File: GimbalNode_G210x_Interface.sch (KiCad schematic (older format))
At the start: 6 parts, among them P1 CONN_01X08_2MNT, P2 CONN_01X08_2MNT, U1 SN74HCT157D, U2 SN74HCT157D

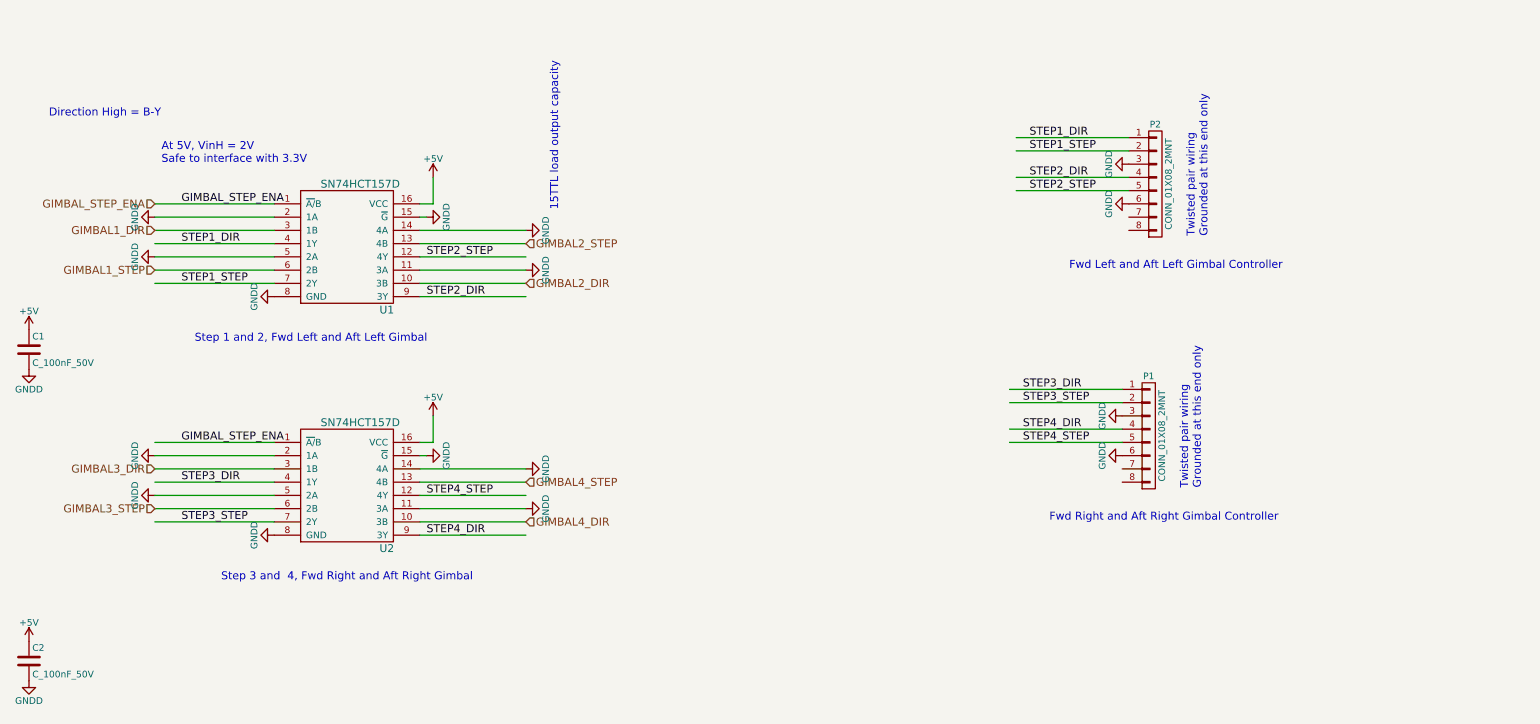
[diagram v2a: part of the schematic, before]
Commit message: Update connectors, diodes, add zener's and anotate.
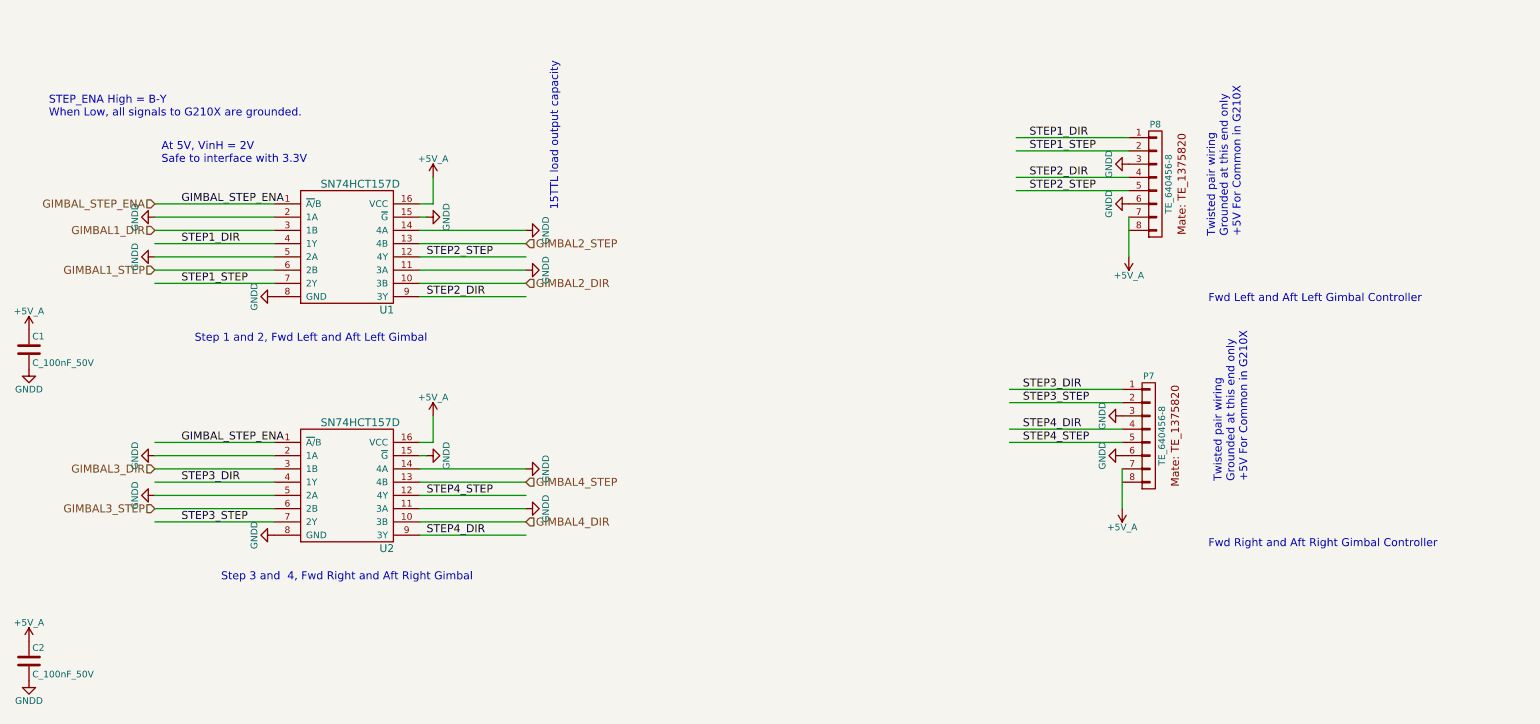
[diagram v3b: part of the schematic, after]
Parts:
- removed P1, P2: CONN_01X08_2MNT, symbol CONN_01X08_2MNT
- added P7, P8: TE_640456-8, RLOOP_FOOTPRINTS:rLoop_TE640456-8, symbol TE_640456-8
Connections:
- net labels added: +5V_A
- net labels removed: +5V
- wire segments 40 -> 42
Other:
- note added: "STEP_ENA High = B-Y\nWhen Low, all signals to G210X are grounded."
- note added: "Twisted pair wiring\nGrounded at this end only\n+5V For Common in G210X"
- note removed: "Direction High = B-Y"
- note removed: "Twisted pair wiring\nGrounded at this end only"
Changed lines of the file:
@@
 $Descr A3 16535 11693
 encoding utf-8
-Sheet 3 6
+Sheet 6 6
 Title "G210 Multiplexers"
 Date ""
@@
 Text Notes 11950 10350 0    118  ~ 0
 rLoop - Gimbal Node\nG210x Multiplexer Interface
-$Comp
-L CONN_01X08_2MNT P2
-U 1 1 5757EB8A
-P 12700 3150
-F 0 "P2" H 12700 3600 50  0000 C CNN
-F 1 "CONN_01X08_2MNT" V 12800 3150 50  0000 C CNN
-F 2 "" H 12700 3150 50  0000 C CNN
-F 3 "" H 12700 3150 50  0000 C CNN
-	1    12700 3150
-	1    0    0    -1
-$EndComp
 Text Notes 5450 4350 0    60   ~ 0
 Step 1 and 2, Fwd Left and Aft Left Gimbal
@@
 	12500 3200 11650 3200
 $Comp
-L GNDD #PWR25
+L GNDD #PWR0102
 U 1 1 5757EB8B
 P 12500 3000
-F 0 "#PWR25" H 12500 2750 50  0001 C CNN
+F 0 "#PWR0102" H 12500 2750 50  0001 C CNN
 F 1 "GNDD" H 12500 2850 50  0000 C CNN
 F 2 "" H 12500 3000 50  0000 C CNN
@@
 $EndComp
 $Comp
-L GNDD #PWR26
+L GNDD #PWR0103
 U 1 1 5757EB8C
 P 12500 3300
-F 0 "#PWR26" H 12500 3050 50  0001 C CNN
+F 0 "#PWR0103" H 12500 3050 50  0001 C CNN
 F 1 "GNDD" H 12500 3150 50  0000 C CNN
 F 2 "" H 12500 3300 50  0000 C CNN
@@
 Text Label 11750 3200 0    60   ~ 0
 STEP2_STEP
-Text Notes 13100 3550 1    60   ~ 0
-Twisted pair wiring\nGrounded at this end only
-$Comp
-L CONN_01X08_2MNT P1
-U 1 1 5757EB8D
-P 12650 5050
-F 0 "P1" H 12650 5500 50  0000 C CNN
-F 1 "CONN_01X08_2MNT" V 12750 5050 50  0000 C CNN
-F 2 "" H 12650 5050 50  0000 C CNN
-F 3 "" H 12650 5050 50  0000 C CNN
-	1    12650 5050
-	1    0    0    -1
-$EndComp
-Text Notes 12050 3800 0    60   ~ 0
+Text Notes 13350 3550 1    60   ~ 0
+Twisted pair wiring\nGrounded at this end only\n+5V For Common in G210X
+Text Notes 13100 4050 0    60   ~ 0
 Fwd Left and Aft Left Gimbal Controller
 Wire Wire Line
@@
 	12450 5100 11600 5100
 $Comp
-L GNDD #PWR23
+L GNDD #PWR0104
 U 1 1 5757EB8E
 P 12450 4900
-F 0 "#PWR23" H 12450 4650 50  0001 C CNN
+F 0 "#PWR0104" H 12450 4650 50  0001 C CNN
 F 1 "GNDD" H 12450 4750 50  0000 C CNN
 F 2 "" H 12450 4900 50  0000 C CNN
@@
 $EndComp
 $Comp
-L GNDD #PWR24
+L GNDD #PWR0105
 U 1 1 5757EB8F
 P 12450 5200
-F 0 "#PWR24" H 12450 4950 50  0001 C CNN
+F 0 "#PWR0105" H 12450 4950 50  0001 C CNN
 F 1 "GNDD" H 12450 5050 50  0000 C CNN
 F 2 "" H 12450 5200 50  0000 C CNN
@@
 Text Label 11700 5100 0    60   ~ 0
 STEP4_STEP
-Text Notes 13050 5450 1    60   ~ 0
-Twisted pair wiring\nGrounded at this end only
-Text Notes 11900 5700 0    60   ~ 0
+Text Notes 13400 5400 1    60   ~ 0
+Twisted pair wiring\nGrounded at this end only\n+5V For Common in G210X
+Text Notes 13100 5900 0    60   ~ 0
 Fwd Right and Aft Right Gimbal Controller
 Text Notes 12000 10500 0    60   ~ 0
@@
 	6050 3900 5150 3900
 $Comp
-L GNDD #PWR15
+L GNDD #PWR0106
 U 1 1 5757EB94
 P 7200 3400
-F 0 "#PWR15" H 7200 3150 50  0001 C CNN
+F 0 "#PWR0106" H 7200 3150 50  0001 C CNN
 F 1 "GNDD" H 7200 3250 50  0000 C CNN
 F 2 "" H 7200 3400 50  0000 C CNN
@@
 	7150 3400 7200 3400
 $Comp
-L GNDD #PWR13
+L GNDD #PWR0107
 U 1 1 5757EB95
 P 6050 4000
-F 0 "#PWR13" H 6050 3750 50  0001 C CNN
+F 0 "#PWR0107" H 6050 3750 50  0001 C CNN
 F 1 "GNDD" H 6050 3850 50  0000 C CNN
 F 2 "" H 6050 4000 50  0000 C CNN
@@
 Text Label 5350 3300 0    60   ~ 0
 GIMBAL_STEP_ENA
-$Comp
-L +5V #PWR17
-U 1 1 5757EB96
-P 7250 3100
-F 0 "#PWR17" H 7250 2950 50  0001 C CNN
-F 1 "+5V" H 7250 3240 50  0000 C CNN
-F 2 "" H 7250 3100 50  0000 C CNN
-F 3 "" H 7250 3100 50  0000 C CNN
-	1    7250 3100
-	1    0    0    -1
-$EndComp
 Wire Wire Line
 	7150 5100 7250 5100
@@
 	6050 5700 5150 5700
 $Comp
-L GNDD #PWR16
+L GNDD #PWR0108
 U 1 1 5757EB98
 P 7200 5200
-F 0 "#PWR16" H 7200 4950 50  0001 C CNN
+F 0 "#PWR0108" H 7200 4950 50  0001 C CNN
 F 1 "GNDD" H 7200 5050 50  0000 C CNN
 F 2 "" H 7200 5200 50  0000 C CNN
@@
 Text Label 5350 5100 0    60   ~ 0
 GIMBAL_STEP_ENA
-$Comp
-L +5V #PWR18
-U 1 1 5757EB9A
-P 7250 4900
-F 0 "#PWR18" H 7250 4750 50  0001 C CNN
-F 1 "+5V" H 7250 5040 50  0000 C CNN
-F 2 "" H 7250 4900 50  0000 C CNN
-F 3 "" H 7250 4900 50  0000 C CNN
-	1    7250 4900
-	1    0    0    -1
-$EndComp
 Text HLabel 5150 3300 0    60   Input ~ 0
 GIMBAL_STEP_ENA
@@
 GIMBAL4_DIR
 Text Notes 4350 2650 0    60   ~ 0
-Direction High = B-Y
+STEP_ENA High = B-Y\nWhen Low, all signals to G210X are grounded.
 Wire Wire Line
 	7150 3800 7950 3800
@@
 STEP4_STEP
 $Comp
-L GNDD #PWR9
+L GNDD #PWR0109
 U 1 1 5757F02C
 P 5150 3400
-F 0 "#PWR9" H 5150 3150 50  0001 C CNN
+F 0 "#PWR0109" H 5150 3150 50  0001 C CNN
 F 1 "GNDD" H 5150 3250 50  0000 C CNN
 F 2 "" H 5150 3400 50  0000 C CNN
@@
 $EndComp
 $Comp
-L GNDD #PWR10
+L GNDD #PWR0110
 U 1 1 5757F037
 P 5150 3700
-F 0 "#PWR10" H 5150 3450 50  0001 C CNN
+F 0 "#PWR0110" H 5150 3450 50  0001 C CNN
 F 1 "GNDD" H 5150 3550 50  0000 C CNN
 F 2 "" H 5150 3700 50  0000 C CNN
@@
 $EndComp
 $Comp
-L GNDD #PWR11
+L GNDD #PWR0111
 U 1 1 5757F042
 P 5150 5200
-F 0 "#PWR11" H 5150 4950 50  0001 C CNN
+F 0 "#PWR0111" H 5150 4950 50  0001 C CNN
 F 1 "GNDD" H 5150 5050 50  0000 C CNN
 F 2 "" H 5150 5200 50  0000 C CNN
@@
 $EndComp
 $Comp
-L GNDD #PWR12
+L GNDD #PWR0112
 U 1 1 5757F04D
 P 5150 5500
-F 0 "#PWR12" H 5150 5250 50  0001 C CNN
+F 0 "#PWR0112" H 5150 5250 50  0001 C CNN
 F 1 "GNDD" H 5150 5350 50  0000 C CNN
 F 2 "" H 5150 5500 50  0000 C CNN
@@
 $EndComp
 $Comp
-L GNDD #PWR19
+L GNDD #PWR0113
 U 1 1 5757F058
 P 7950 3500
-F 0 "#PWR19" H 7950 3250 50  0001 C CNN
+F 0 "#PWR0113" H 7950 3250 50  0001 C CNN
 F 1 "GNDD" H 7950 3350 50  0000 C CNN
 F 2 "" H 7950 3500 50  0000 C CNN
@@
 $EndComp
 $Comp
-L GNDD #PWR20
+L GNDD #PWR0114
 U 1 1 5757F063
 P 7950 3800
-F 0 "#PWR20" H 7950 3550 50  0001 C CNN
+F 0 "#PWR0114" H 7950 3550 50  0001 C CNN
 F 1 "GNDD" H 7950 3650 50  0000 C CNN
 F 2 "" H 7950 3800 50  0000 C CNN
@@
 $EndComp
 $Comp
-L GNDD #PWR21
+L GNDD #PWR0115
 U 1 1 5757F078
 P 7950 5300
-F 0 "#PWR21" H 7950 5050 50  0001 C CNN
+F 0 "#PWR0115" H 7950 5050 50  0001 C CNN
 F 1 "GNDD" H 7950 5150 50  0000 C CNN
 F 2 "" H 7950 5300 50  0000 C CNN
@@
 $EndComp
 $Comp
-L GNDD #PWR22
+L GNDD #PWR0116
 U 1 1 5757F083
 P 7950 5600
-F 0 "#PWR22" H 7950 5350 50  0001 C CNN
+F 0 "#PWR0116" H 7950 5350 50  0001 C CNN
 F 1 "GNDD" H 7950 5450 50  0000 C CNN
 F 2 "" H 7950 5600 50  0000 C CNN
@@
 $EndComp
 $Comp
-L GNDD #PWR14
+L GNDD #PWR0117
 U 1 1 5758A913
 P 6050 5800
-F 0 "#PWR14" H 6050 5550 50  0001 C CNN
+F 0 "#PWR0117" H 6050 5550 50  0001 C CNN
 F 1 "GNDD" H 6050 5650 50  0000 C CNN
 F 2 "" H 6050 5800 50  0000 C CNN
@@
 $EndComp
 $Comp
-L GNDD #PWR6
+L GNDD #PWR0118
 U 1 1 5758AA2C
 P 4200 4550
-F 0 "#PWR6" H 4200 4300 50  0001 C CNN
+F 0 "#PWR0118" H 4200 4300 50  0001 C CNN
 F 1 "GNDD" H 4200 4400 50  0000 C CNN
 F 2 "" H 4200 4550 50  0000 C CNN
@@
 $EndComp
 $Comp
-L +5V #PWR5
-U 1 1 5758AA38
-P 4200 4250
-F 0 "#PWR5" H 4200 4100 50  0001 C CNN
-F 1 "+5V" H 4200 4390 50  0000 C CNN
-F 2 "" H 4200 4250 50  0000 C CNN
-F 3 "" H 4200 4250 50  0000 C CNN
-	1    4200 4250
-	1    0    0    -1
-$EndComp
-$Comp
-L GNDD #PWR8
+L GNDD #PWR0119
 U 1 1 5758AAB6
 P 4200 6900
-F 0 "#PWR8" H 4200 6650 50  0001 C CNN
+F 0 "#PWR0119" H 4200 6650 50  0001 C CNN
 F 1 "GNDD" H 4200 6750 50  0000 C CNN
 F 2 "" H 4200 6900 50  0000 C CNN
 F 3 "" H 4200 6900 50  0000 C CNN
 	1    4200 6900
-	1    0    0    -1
-$EndComp
-$Comp
-L +5V #PWR7
-U 1 1 5758AAC2
-P 4200 6600
-F 0 "#PWR7" H 4200 6450 50  0001 C CNN
-F 1 "+5V" H 4200 6740 50  0000 C CNN
-F 2 "" H 4200 6600 50  0000 C CNN
-F 3 "" H 4200 6600 50  0000 C CNN
-	1    4200 6600
 	1    0    0    -1
 $EndComp
@@
 	1    0    0    -1
 $EndComp
+$Comp
+L +5V_A #PWR0120
+U 1 1 575C1A3E
+P 7250 3100
+F 0 "#PWR0120" H 7250 2950 50  0001 C CNN
+F 1 "+5V_A" H 7250 3240 50  0000 C CNN
+F 2 "" H 7250 3100 60  0000 C CNN
+F 3 "" H 7250 3100 60  0000 C CNN
+	1    7250 3100
+	1    0    0    -1
+$EndComp
+$Comp
+L +5V_A #PWR0121
+U 1 1 575C1A62
+P 7250 4900
+F 0 "#PWR0121" H 7250 4750 50  0001 C CNN
+F 1 "+5V_A" H 7250 5040 50  0000 C CNN
+F 2 "" H 7250 4900 60  0000 C CNN
+F 3 "" H 7250 4900 60  0000 C CNN
+	1    7250 4900
+	1    0    0    -1
+$EndComp
+$Comp
+L +5V_A #PWR0122
+U 1 1 575C1A80
+P 4200 4250
+F 0 "#PWR0122" H 4200 4100 50  0001 C CNN
+F 1 "+5V_A" H 4200 4390 50  0000 C CNN
+F 2 "" H 4200 4250 60  0000 C CNN
+F 3 "" H 4200 4250 60  0000 C CNN
+	1    4200 4250
+	1    0    0    -1
+$EndComp
+$Comp
+L +5V_A #PWR0123
+U 1 1 575C1A8E
+P 4200 6600
+F 0 "#PWR0123" H 4200 6450 50  0001 C CNN
+F 1 "+5V_A" H 4200 6740 50  0000 C CNN
+F 2 "" H 4200 6600 60  0000 C CNN
+F 3 "" H 4200 6600 60  0000 C CNN
+	1    4200 6600
+	1    0    0    -1
+$EndComp
+$Comp
+L TE_640456-8 P8
+U 1 1 575C59A8
+P 12650 2750
+F 0 "P8" H 12700 2800 50  0000 C CNN
+F 1 "TE_640456-8" V 12800 2350 50  0000 C CNN
+F 2 "RLOOP_FOOTPRINTS:rLoop_TE640456-8" H 12700 2350 50  0001 C CNN
+F 3 "" H 12700 2350 50  0000 C CNN
+	1    12650 2750
+	1    0    0    -1
+$EndComp
+$Comp
+L TE_640456-8 P7
+U 1 1 575C5A11
+P 12600 4650
+F 0 "P7" H 12650 4700 50  0000 C CNN
+F 1 "TE_640456-8" V 12750 4250 50  0000 C CNN
+F 2 "RLOOP_FOOTPRINTS:rLoop_TE640456-8" H 12650 4250 50  0001 C CNN
+F 3 "" H 12650 4250 50  0000 C CNN
+	1    12600 4650
+	1    0    0    -1
+$EndComp
+$Comp
+L +5V_A #PWR0124
+U 1 1 575C5A1D
+P 12450 5600
+F 0 "#PWR0124" H 12450 5450 50  0001 C CNN
+F 1 "+5V_A" H 12450 5740 50  0000 C CNN
+F 2 "" H 12450 5600 60  0000 C CNN
+F 3 "" H 12450 5600 60  0000 C CNN
+	1    12450 5600
+	-1   0    0    1
+$EndComp
+Wire Wire Line
+	12450 5300 12450 5600
+$Comp
+L +5V_A #PWR0125
+U 1 1 575C5AFF
+P 12500 3700
+F 0 "#PWR0125" H 12500 3550 50  0001 C CNN
+F 1 "+5V_A" H 12500 3840 50  0000 C CNN
+F 2 "" H 12500 3700 60  0000 C CNN
+F 3 "" H 12500 3700 60  0000 C CNN
+	1    12500 3700
+	-1   0    0    1
+$EndComp
+Wire Wire Line
+	12500 3400 12500 3700
 $EndSCHEMATC
